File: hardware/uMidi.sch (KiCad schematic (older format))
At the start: 55 parts, among them CON1 USB-MINI-B, IC1 ATXMEGA128A4U-M, IC2 74LS14, IC3 LT1129CST-3.3, IC4 6N138, P1 MIDI In, P2 MIDI Thru, P3 MIDI T/O, P4 MIDI Out, P5 5..12 V, P6 PDI, P7 GPIO1, P8 GPIO2, P9 GPIO2

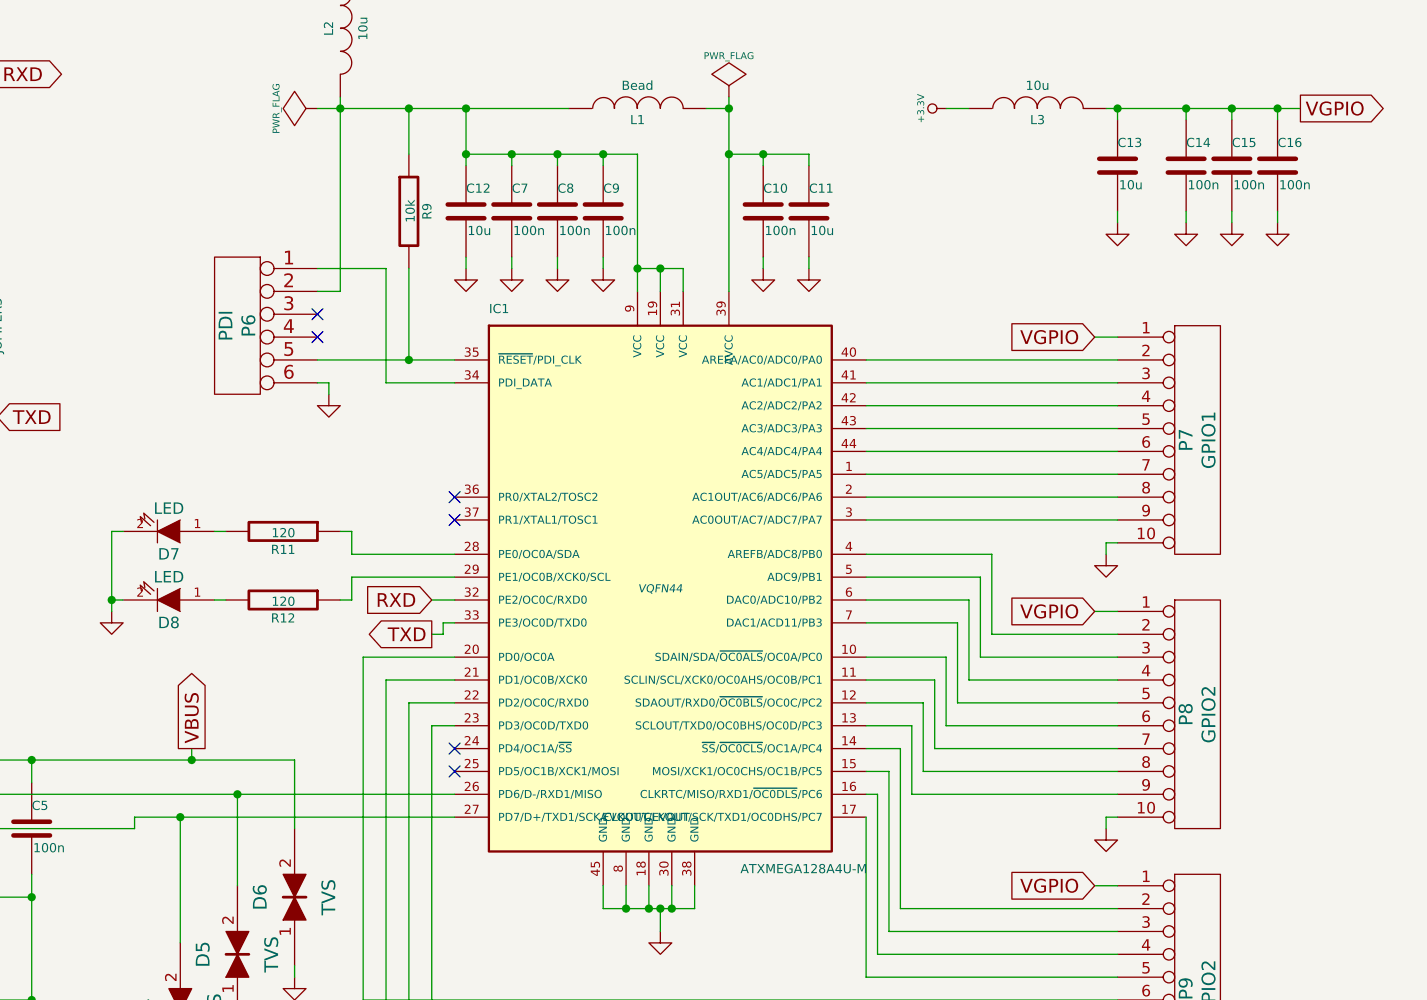
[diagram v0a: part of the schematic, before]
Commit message: Add TWI pullup resistors
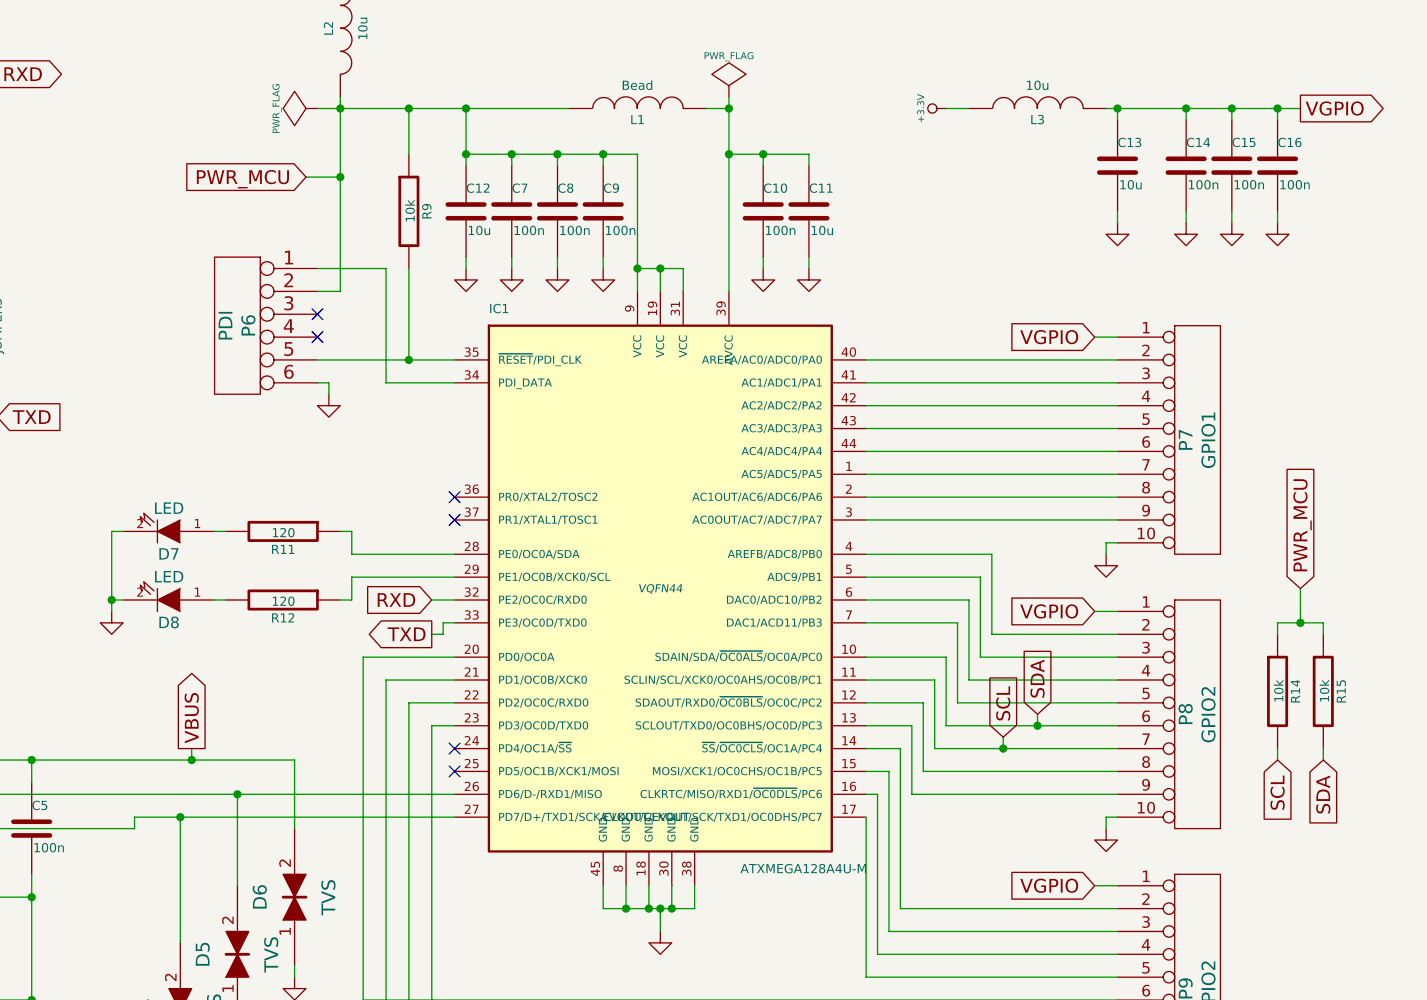
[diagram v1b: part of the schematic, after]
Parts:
- added R14, R15: 10k, symbol R
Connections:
- net SDA: now reaches IC1.10 (SDAIN/SDA/~OC0ALS~/OC0A/PC0), P8.6 (P6)
- net SDA: now also R15.2
- net SCL: now reaches IC1.11 (SCLIN/SCL/XCK0/OC0AHS/OC0B/PC1), P8.7 (P7)
- net SCL: now also R14.2
- net PWR_MCU: now reaches C12.1, C7.1, C8.1, C9.1, IC1.19 (VCC), IC1.31 (VCC), IC1.9 (VCC), L1.1, L2.2, P6.2, R9.1
- net PWR_MCU: now also R14.1, R15.1
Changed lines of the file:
@@
+	1    0    0    -1
+$EndComp
+$Comp
+L R R14
+U 1 1 5484813F
+P 9900 4200
+F 0 "R14" V 9980 4200 40  0000 C CNN
+F 1 "10k" V 9907 4201 40  0000 C CNN
+F 2 "" V 9830 4200 30  0000 C CNN
+F 3 "" H 9900 4200 30  0000 C CNN
+	1    9900 4200
+	1    0    0    -1
+$EndComp
+$Comp
+L R R15
+U 1 1 548484DC
+P 10100 4200
+F 0 "R15" V 10180 4200 40  0000 C CNN
+F 1 "10k" V 10107 4201 40  0000 C CNN
+F 2 "" V 10030 4200 30  0000 C CNN
+F 3 "" H 10100 4200 30  0000 C CNN
+	1    10100 4200
 	1    0    0    -1
 $EndComp
@@
 Wire Wire Line
 	3300 1150 3300 1200
+Text GLabel 9900 4500 3    60   Input ~ 0
+SCL
+Text GLabel 8850 4300 1    60   Input ~ 0
+SDA
+Text GLabel 8700 4400 1    60   Input ~ 0
+SCL
+Text GLabel 10100 4500 3    60   Input ~ 0
+SDA
+Wire Wire Line
+	9900 4500 9900 4450
+Wire Wire Line
+	10100 4500 10100 4450
+Wire Wire Line
+	9900 3900 10100 3900
+Wire Wire Line
+	9900 3900 9900 3950
+Wire Wire Line
+	10100 3900 10100 3950
+Connection ~ 10000 3900
+Wire Wire Line
+	8850 4300 8850 4350
+Connection ~ 8850 4350
+Wire Wire Line
+	8700 4400 8700 4450
+Connection ~ 8700 4450
+Text GLabel 5650 1950 0    60   Input ~ 0
+PWR_MCU
+Wire Wire Line
+	5650 1950 5800 1950
+Connection ~ 5800 1950
+Text GLabel 10000 3750 1    60   Input ~ 0
+PWR_MCU
+Wire Wire Line
+	10000 3900 10000 3750
 $EndSCHEMATC

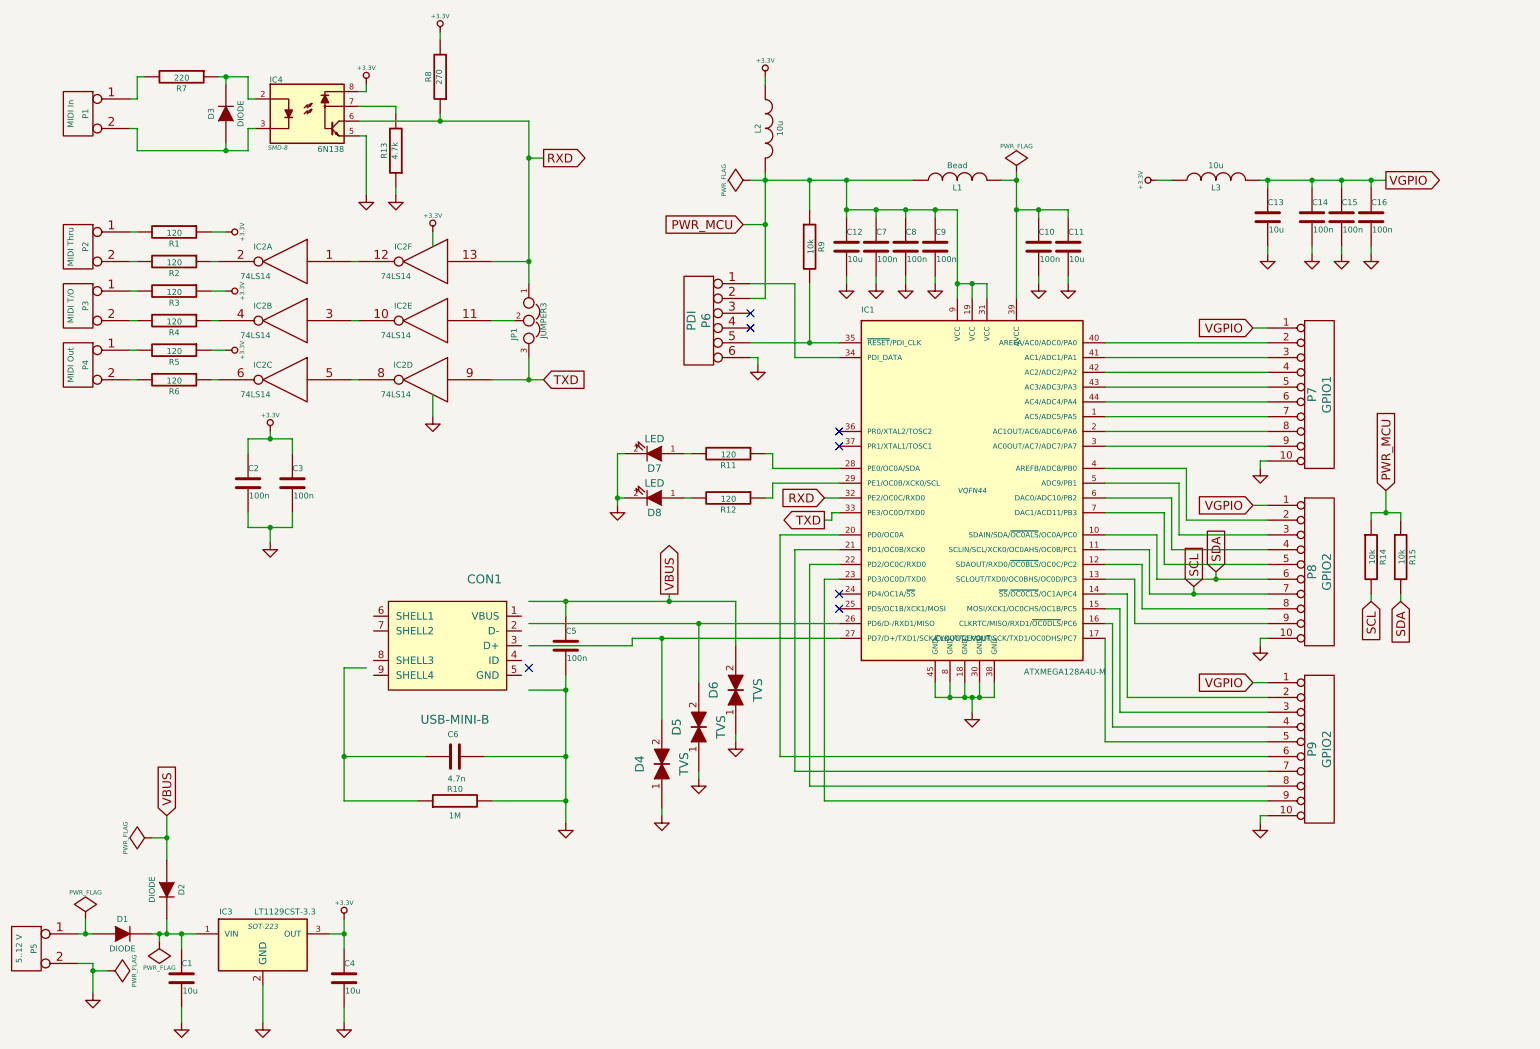
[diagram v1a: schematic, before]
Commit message: Add solder jumpers to yet unused GPIO pins
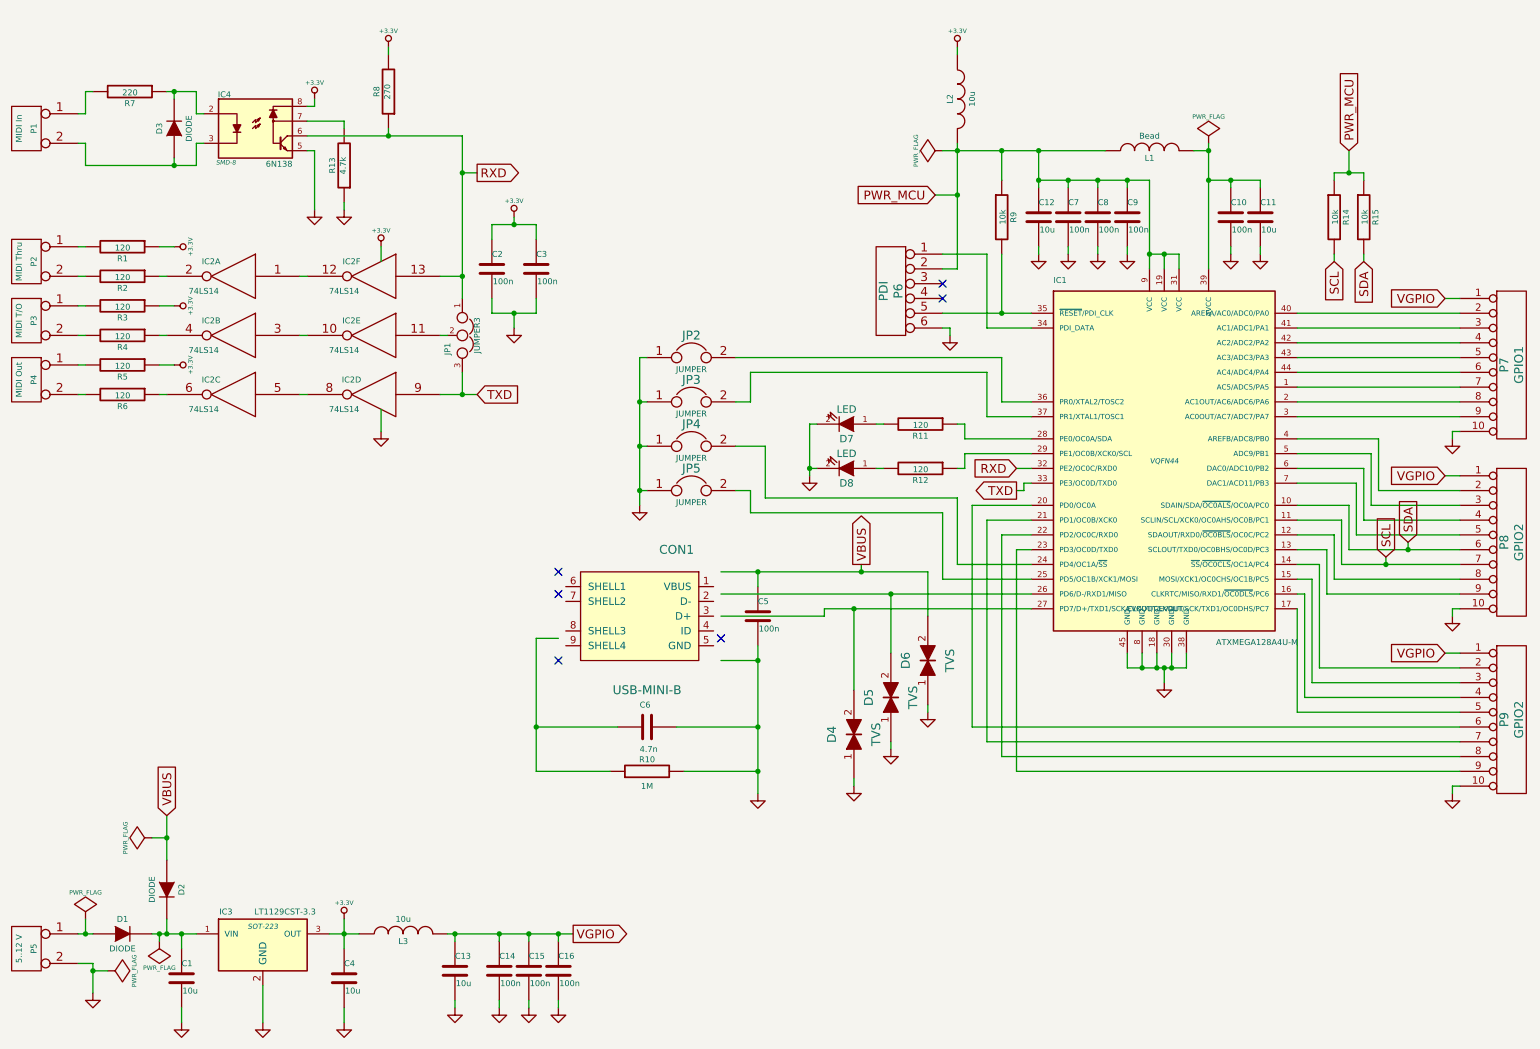
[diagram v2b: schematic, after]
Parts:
- added JP2, JP3, JP4, JP5: JUMPER, symbol JUMPER
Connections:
- net GND: now also JP2.1, JP3.1, JP4.1, JP5.1
- net at IC1.24 (PD4/OC1A/~SS~): now also JP4.2
- net at IC1.25 (PD5/OC1B/XCK1/MOSI): now also JP5.2
- net at IC1.36 (PR0/XTAL2/TOSC2): now also JP2.2
- net at IC1.37 (PR1/XTAL1/TOSC1): now also JP3.2
- no-connect marks 7 -> 6
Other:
- moved on the sheet: C10, C11, C12, C13, C14, C15, C16, C2, C3, C5, C6, C7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

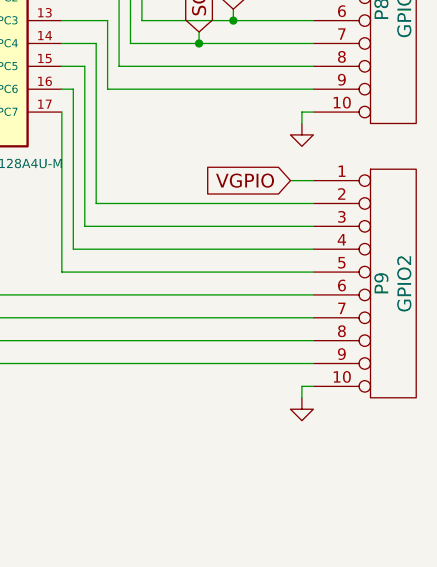
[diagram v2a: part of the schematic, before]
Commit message: Fix GPIO3 value and silkscreen text
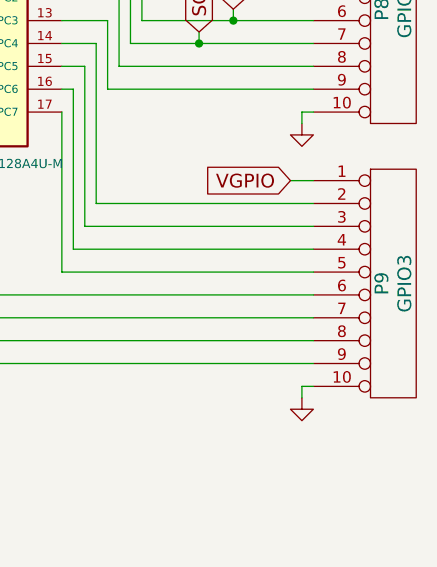
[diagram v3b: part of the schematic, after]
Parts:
- P9: value GPIO2 -> GPIO3
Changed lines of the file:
@@
 P 10850 5300
 F 0 "P9" V 10800 5300 60  0000 C CNN
-F 1 "GPIO2" V 10900 5300 60  0000 C CNN
+F 1 "GPIO3" V 10900 5300 60  0000 C CNN
 F 2 "" H 10850 5300 60  0000 C CNN
 F 3 "" H 10850 5300 60  0000 C CNN
